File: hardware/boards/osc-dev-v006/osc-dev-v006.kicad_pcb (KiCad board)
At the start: 4 copper layers, 60 x 60 mm, 92 parts, among them J1 JST-PH-H, J10 PIN-1-3P, J11 JST-PH-V, J2 TERM, J3 PIN-1-3P, J4 PIN-2-3P, J5 JST-ZH-H, J6 PIN-1-2P, J7 PIN-1-5P, J8 PIN-2-2P, J9 PIN-1-3P, U1 HT7533-1, U2 DRV8212PDSGR, U3 CH32V006F8P6, U4 74LVC2G241

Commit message: OSC DEV V006 Rev B touch up (#12)
* add logo and QR code to pcb, added logo to readme. updated board front side screenshot

* responsive logo

* optimize image
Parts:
- moved C10 7.40 mm to (162.1, 96.7), turned to 90 degrees
- moved C9 4.43 mm to (164.1, 96.7), turned to 90 degrees
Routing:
- net /TX: track 66.2 -> 68.8 mm
- net /DBG: track 46.9 -> 48.1 mm
- net GND: track 27.5 -> 26.3 mm, vias 74 -> 69
- net /ISNS+: track 23.7 -> 24.7 mm
- net +3V3: track 22.9 -> 21.9 mm
- net /TX_EN: track 45.9 -> 46.6 mm
- net /VNTC: track 41.5 -> 42.2 mm
- net VSYS: track 99.7 -> 100.3 mm
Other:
- board text added: "OSC Dev V006 Rev. B"
- board text removed: "HDR 2X2P"
- board text removed: "HDR 2X3P"
- board text removed: "HDR-2P"
- board text removed: "HDR-3P"
- board text removed: "HDR-5P"
- board text removed: "JST-PH-3P"
- board text removed: "M2 Ø2.2"
- board text removed: "MCU: CH32V006F8P6 DRV: DRV8212PDSGR LDO: HT7533-1 BUF: 74LVC2G241 RS1: 10mOhm ~1% 333mW"
- board text removed: "OSC Dev V006 Rev. B Feb. 2026"
- board text removed: "OpenServoCore"
- board text removed: "https://github.com/OpenServoCore"

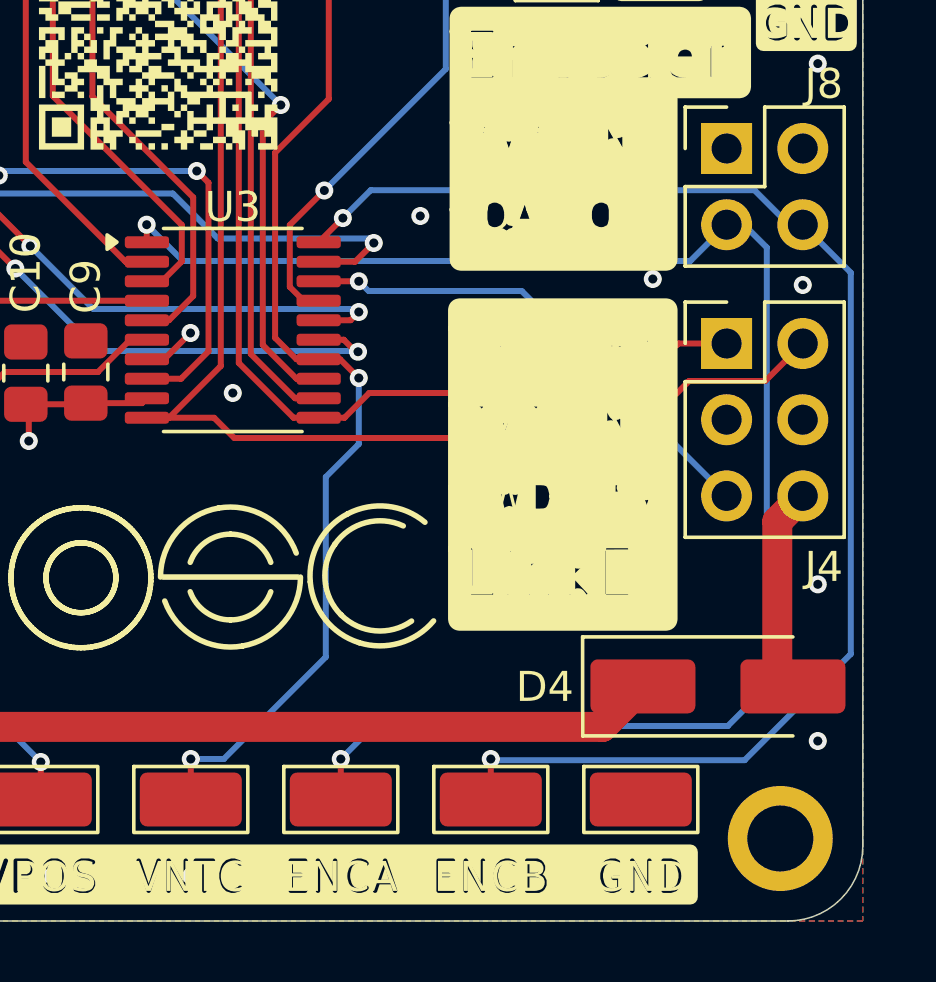
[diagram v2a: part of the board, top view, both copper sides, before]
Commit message: final check and swapping ENCA/ENCB
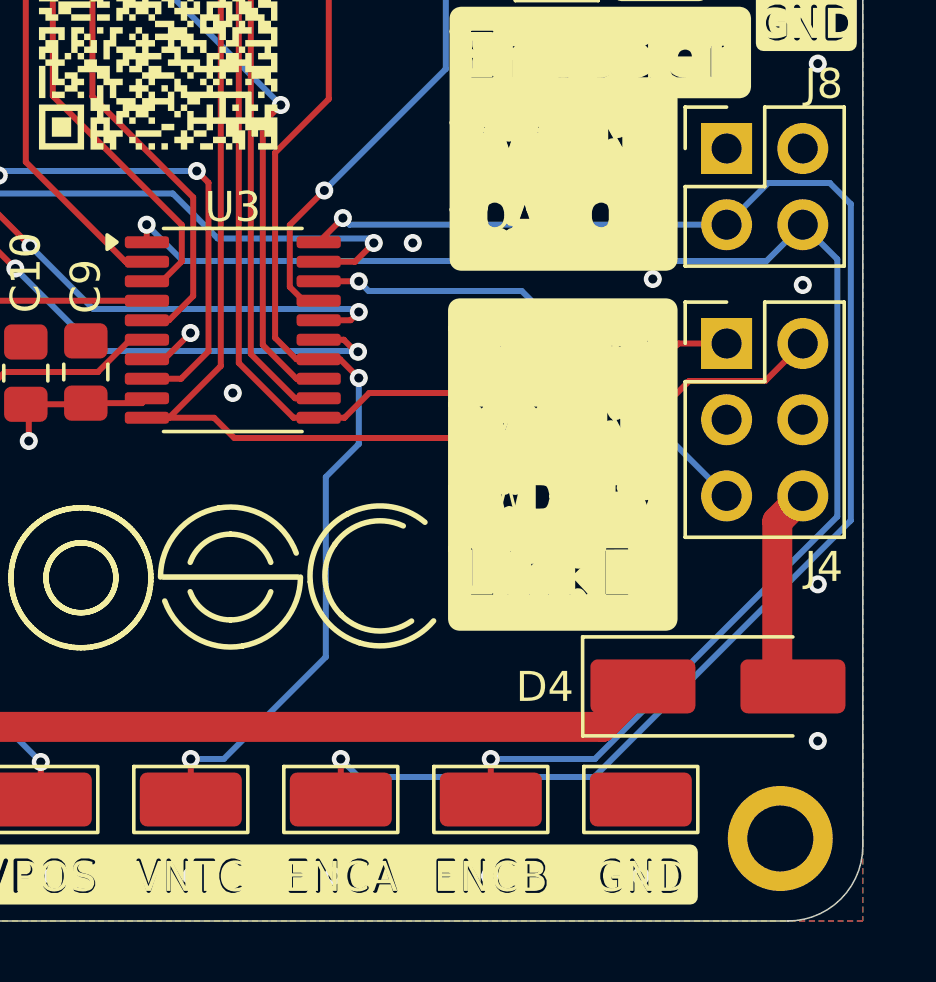
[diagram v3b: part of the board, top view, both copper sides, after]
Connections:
- U3 pad 1: /ENCA -> /ENCB
- U3 pad 20: /ENCB -> /ENCA
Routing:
- net /ENCB: track 47.2 -> 49.9 mm
- net /ENCA: track 53.8 -> 51.7 mm
- net GND: vias 69 -> 72
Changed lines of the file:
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@@
 			(layers "F.Cu" "F.Mask" "F.Paste")
 			(roundrect_rratio 0.25)
-			(net "/ENCA")
+			(net "/ENCB")
 			(pinfunction "A7_1")
 			(pintype "passive")
@@
 			(layers "F.Cu" "F.Mask" "F.Paste")
 			(roundrect_rratio 0.25)
-			(net "/ENCB")
+			(net "/ENCA")
 			(pinfunction "A4_20")
 			(pintype "passive")
@@
 	)
 	(via
-		(at 175.25 91.5)
+		(at 175 92.4)
 		(size 0.6)
 		(drill 0.3)
@@
 	)
 	(via
+		(at 182.6 113.5)
+		(size 0.6)
+		(drill 0.3)
+		(layers "F.Cu" "B.Cu")
+		(free yes)
+		(capping no)
+		(covering
+			(front no)
+			(back no)
+		)
+		(plugging
+			(front no)
+			(back no)
+		)
+		(filling no)
+		(net "GND")
+	)
+	(via
 		(at 175.5 77.3)
 		(size 0.6)
@@
 	)
 	(via
+		(at 172.344444 113.5)
+		(size 0.6)
+		(drill 0.3)
+		(layers "F.Cu" "B.Cu")
+		(free yes)
+		(capping no)
+		(covering
+			(front no)
+			(back no)
+		)
+		(plugging
+			(front no)
+			(back no)
+		)
+		(filling no)
+		(net "GND")
+	)
+	(via
 		(at 188.5 103.777778)
 		(size 0.6)
@@
 	)
 	(via
+		(at 177.572222 113.5)
+		(size 0.6)
+		(drill 0.3)
+		(layers "F.Cu" "B.Cu")
+		(free yes)
+		(capping no)
+		(covering
+			(front no)
+			(back no)
+		)
+		(plugging
+			(front no)
+			(back no)
+		)
+		(filling no)
+		(net "GND")
+	)
+	(via
 		(at 159.5 77.1)
 		(size 0.6)
@@
 	)
 	(segment
-		(start 171.8625 92.375)
-		(end 172.66875 91.56875)
+		(start 166.13 91.79)
+		(end 166.13 92.3675)
 		(width 0.2)
 		(layer "F.Cu")
@@
 	)
 	(segment
-		(start 177.6 110.975)
-		(end 177.6 109.6)
+		(start 166.13 92.3675)
+		(end 166.1375 92.375)
 		(width 0.2)
 		(layer "F.Cu")
 		(net "/ENCB")
 	)
-	(via
-		(at 172.66875 91.56875)
-		(size 0.6)
-		(drill 0.3)
-		(layers "F.Cu" "B.Cu")
+	(segment
+		(start 177.6 110.975)
+		(end 177.6 109.6)
+		(width 0.2)
+		(layer "F.Cu")
 		(net "/ENCB")
 	)
@@
 		(net "/ENCB")
 	)
-	(segment
-		(start 173.5975 90.64)
-		(end 186.39 90.64)
-		(width 0.2)
-		(layer "B.Cu")
-		(net "/ENCB")
-	)
-	(segment
-		(start 186.39 90.64)
-		(end 187.54 91.79)
-		(width 0.2)
-		(layer "B.Cu")
+	(via
+		(at 166.13 91.79)
+		(size 0.6)
+		(drill 0.3)
+		(layers "F.Cu" "B.Cu")
 		(net "/ENCB")
 	)
 	(segment
-		(start 188 91.79)
-		(end 189.6 93.39)
+		(start 189.15 92.94)
+		(end 189.15 101.519939)
 		(width 0.2)
 		(layer "B.Cu")
@@
 	)
 	(segment
-		(start 186.06 109.64)
-		(end 177.56 109.64)
+		(start 186.79 93)
+		(end 188 91.79)
 		(width 0.2)
 		(layer "B.Cu")
@@
 	)
 	(segment
-		(start 177.56 109.64)
-		(end 177.55 109.65)
+		(start 188 91.79)
+		(end 189.15 92.94)
 		(width 0.2)
 		(layer "B.Cu")
@@
 	)
 	(segment
-		(start 189.6 106.1)
-		(end 186.06 109.64)
+		(start 181.069939 109.6)
+		(end 177.6 109.6)
 		(width 0.2)
 		(layer "B.Cu")
@@
 	)
 	(segment
-		(start 172.66875 91.56875)
-		(end 173.5975 90.64)
+		(start 189.15 101.519939)
+		(end 181.069939 109.6)
 		(width 0.2)
 		(layer "B.Cu")
@@
 	)
 	(segment
-		(start 187.54 91.79)
-		(end 188 91.79)
+		(start 166.13 91.79)
+		(end 167.34 93)
 		(width 0.2)
 		(layer "B.Cu")
@@
 	)
 	(segment
-		(start 189.6 93.39)
-		(end 189.6 106.1)
+		(start 167.34 93)
+		(end 186.79 93)
 		(width 0.2)
 		(layer "B.Cu")
@@
 	)
 	(segment
-		(start 166.13 91.79)
-		(end 166.13 92.3675)
-		(width 0.2)
-		(layer "F.Cu")
-		(net "/ENCA")
-	)
-	(segment
-		(start 166.13 92.3675)
-		(end 166.1375 92.375)
+		(start 171.8625 92.375)
+		(end 172.66875 91.56875)
 		(width 0.2)
 		(layer "F.Cu")
@@
 	)
 	(via
-		(at 166.13 91.79)
+		(at 172.66875 91.56875)
 		(size 0.6)
 		(drill 0.3)
 		(layers "F.Cu" "B.Cu")
-		(free yes)
 		(net "/ENCA")
 	)
 	(segment
-		(start 185.46 91.79)
-		(end 186.04 91.79)
+		(start 172.66875 91.56875)
+		(end 172.89 91.79)
 		(width 0.2)
 		(layer "B.Cu")
@@
 	)
 	(segment
-		(start 185.5 108.5)
-		(end 173.7 108.5)
+		(start 181.05 110.2)
+		(end 173.2 110.2)
 		(width 0.2)
 		(layer "B.Cu")
@@
 	)
 	(segment
-		(start 173.7 108.5)
-		(end 172.55 109.65)
+		(start 189.6 91.1)
+		(end 189.6 101.65)
 		(width 0.2)
 		(layer "B.Cu")
@@
 	)
 	(segment
-		(start 186.8 107.2)
-		(end 185.5 108.5)
+		(start 172.89 91.79)
+		(end 185.46 91.79)
 		(width 0.2)
 		(layer "B.Cu")
@@
 	)
 	(segment
-		(start 186.04 91.79)
-		(end 186.8 92.55)
+		(start 189.6 101.65)
+		(end 181.05 110.2)
 		(width 0.2)
 		(layer "B.Cu")
@@
 	)
 	(segment
-		(start 184.25 93)
-		(end 185.46 91.79)
+		(start 186.85 90.4)
+		(end 188.9 90.4)
 		(width 0.2)
 		(layer "B.Cu")
@@
 	)
 	(segment
-		(start 166.13 91.79)
-		(end 167.34 93)
+		(start 188.9 90.4)
+		(end 189.6 91.1)
 		(width 0.2)
 		(layer "B.Cu")
@@
 	)
 	(segment
-		(start 167.34 93)
-		(end 184.25 93)
+		(start 185.46 91.79)
+		(end 186.85 90.4)
 		(width 0.2)
 		(layer "B.Cu")
@@
 	)
 	(segment
-		(start 186.8 92.55)
-		(end 186.8 107.2)
+		(start 173.2 110.2)
+		(end 172.6 109.6)
 		(width 0.2)
 		(layer "B.Cu")

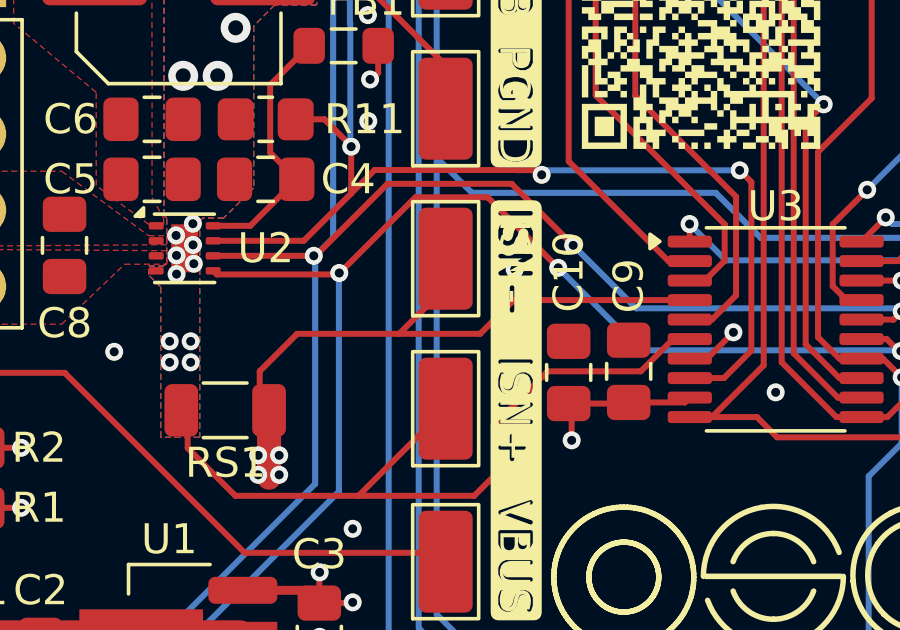
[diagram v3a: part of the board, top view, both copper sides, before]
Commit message: OSC Dev V006 Rev B patch (#21)
* osc-dev-v006: add SB1 bootstrap bridge for nRST/OPN

* osc-dev-v006: docs — Rev B validated, SB1 in-rev patch
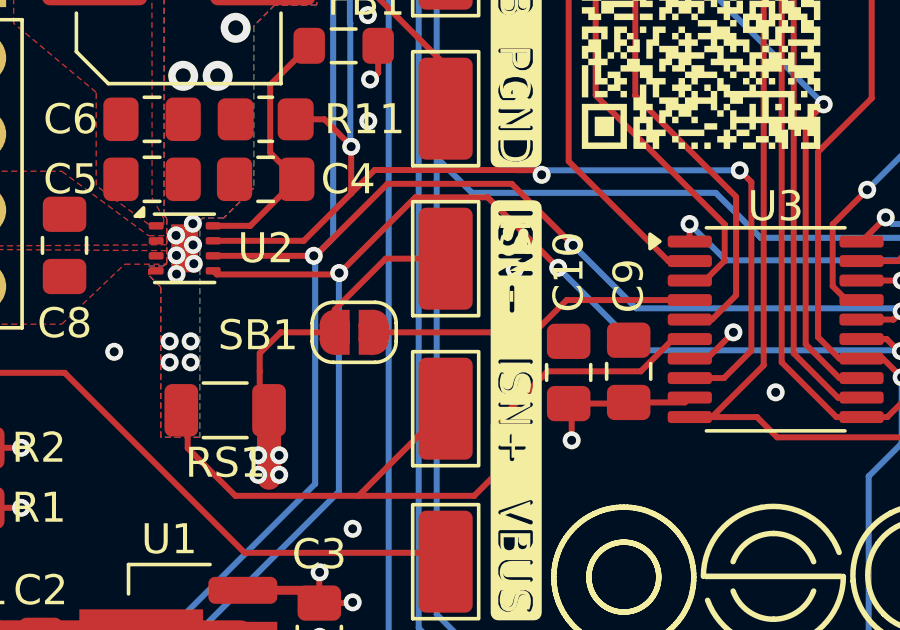
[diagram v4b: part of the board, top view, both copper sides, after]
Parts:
- added SB1: Bootstrap, Jumper:SolderJumper-2_P1.3mm_Open_RoundedPad1.0x1.5mm, F.Cu at (154.9, 95.4)
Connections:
- U3 pad 4: /ISNS- -> /MCU/OPN2
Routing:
- net /MCU/OPN2: track 0.00 -> 11.4 mm
- net /ISNS-: track 18.5 -> 9.15 mm
